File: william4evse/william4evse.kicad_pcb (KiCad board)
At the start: 2 copper layers, 34 x 66 mm, 2 parts, among them J1 Boom_Precision_RJ45-B-1x1, U1 RCMB121

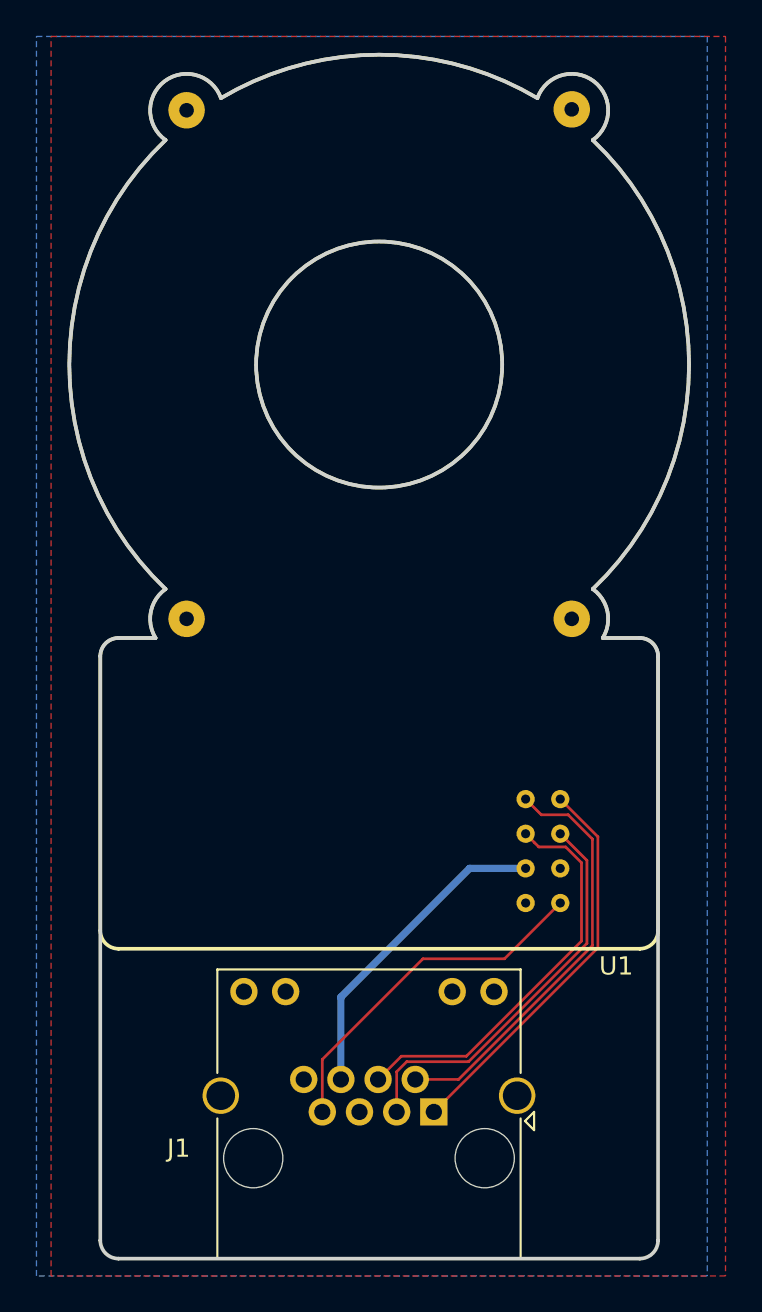
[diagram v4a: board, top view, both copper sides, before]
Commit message: william: Misc updates
- Add power inductor in the power line
- Swap TEST_IN and X30_OUT signals
- Fix board outline to take RCMB bumps into account
- Fix RCMB hole size
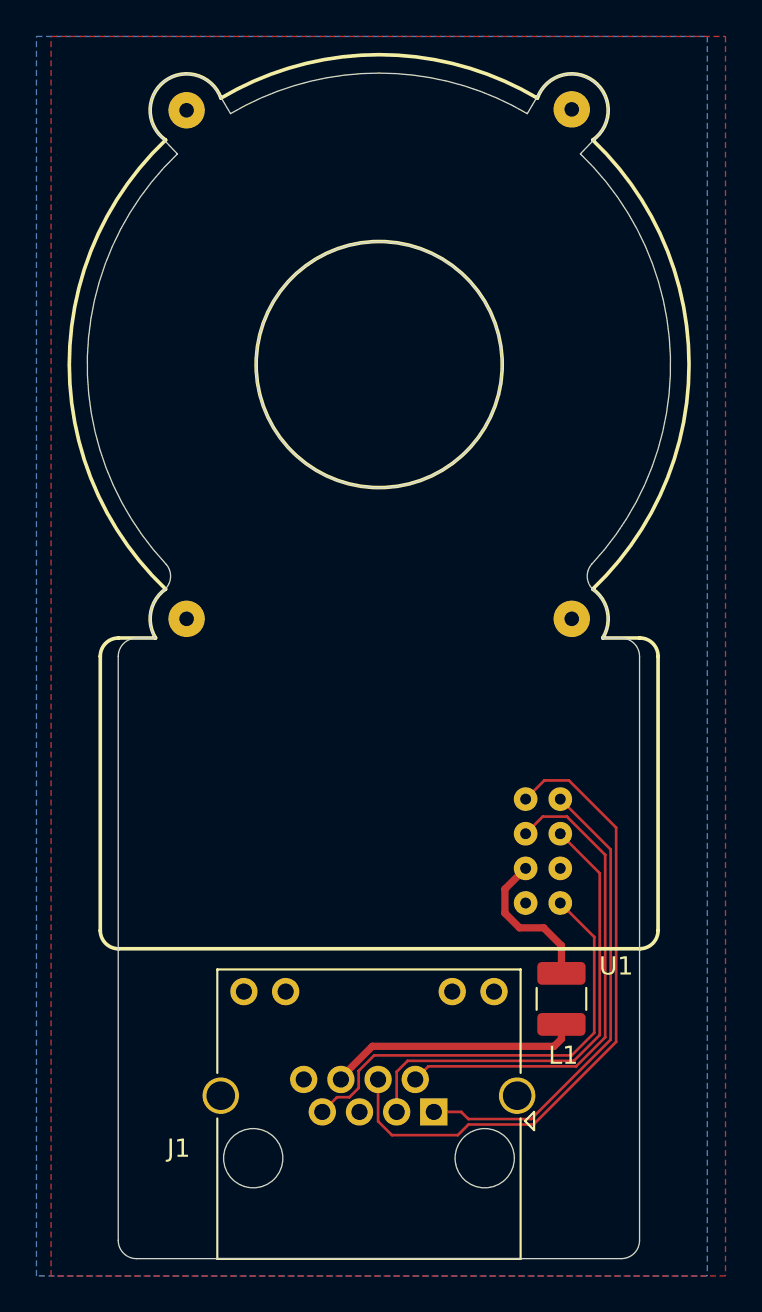
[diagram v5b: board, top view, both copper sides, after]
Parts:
- added L1: 220uH, Inductor_SMD:L_1210_3225Metric, F.Cu at (152.0, 108.8)
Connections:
- J1 pad 2: /TEST_IN -> /X30_OUT
- J1 pad 4: /X30_OUT -> /TEST_IN
- U1 pad 6: +5V -> Net-(L1-Pad2)
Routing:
- net /TEST_IN: track 23.2 -> 36.0 mm
- net Net-(L1-Pad2): track 0.00 -> 8.29 mm
- net /PWM_OUT: track 19.5 -> 25.2 mm
- net /X30_OUT: track 22.3 -> 27.0 mm
- net /ERROR_OUT: track 21.7 -> 26.0 mm
- net /X6_OUT: track 22.2 -> 26.1 mm
- net +5V: track 17.6 -> 13.9 mm
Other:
- board size 34 x 66 mm -> 32 x 65 mm

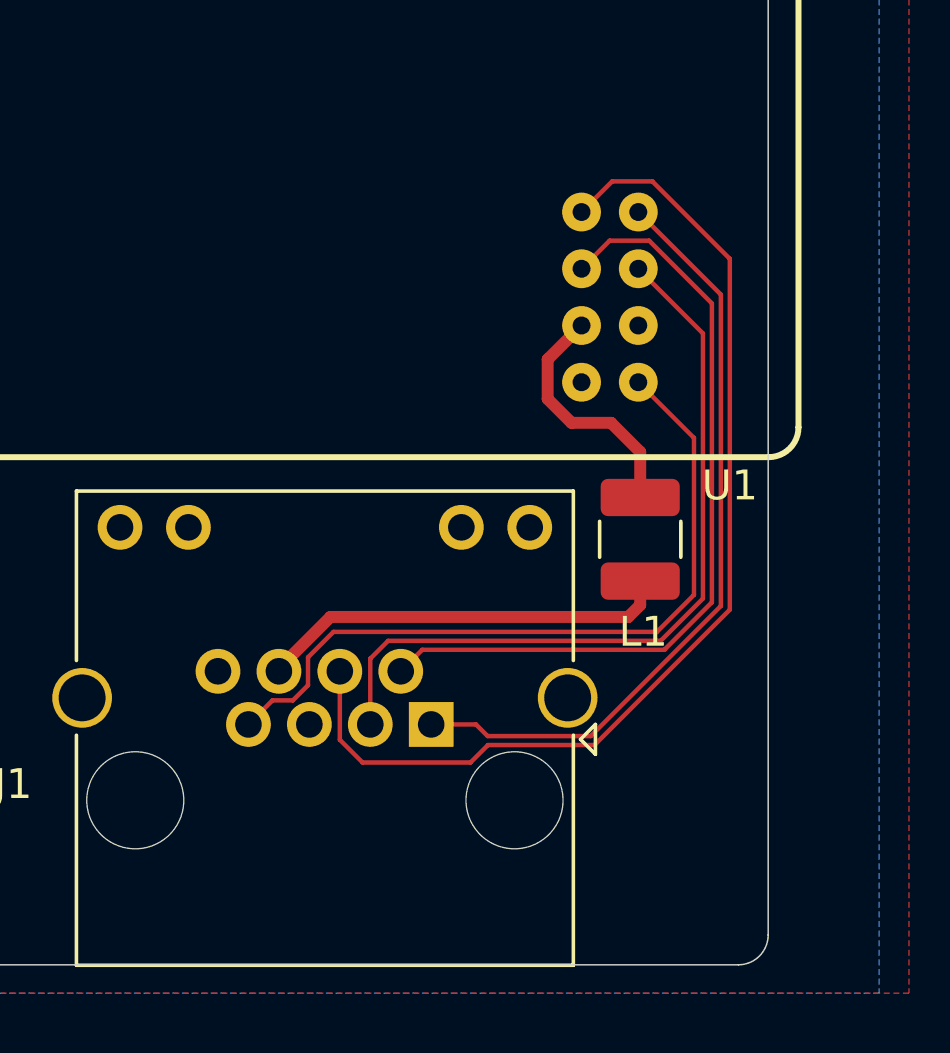
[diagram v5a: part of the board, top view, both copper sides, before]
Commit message: william{sch, pcb}: Swap (again) wires
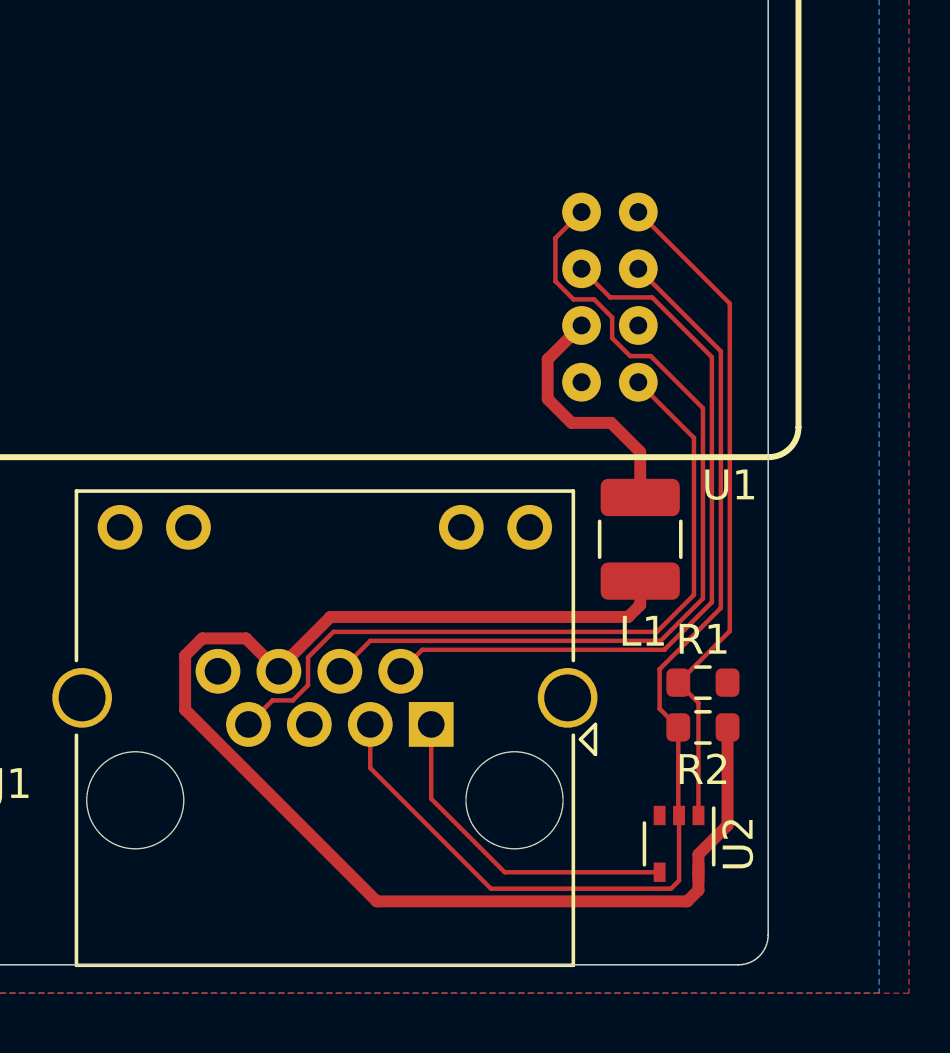
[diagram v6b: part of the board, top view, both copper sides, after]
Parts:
- added R1: 10k, Resistor_SMD:R_0603_1608Metric, F.Cu at (154.1, 113.6)
- added R2: 10k, Resistor_SMD:R_0603_1608Metric, F.Cu at (154.1, 115.1)
- added U2: 74LVC1G32, Package_TO_SOT_SMD:SOT-353_SC-70-5, F.Cu at (153.3, 119.0)
- L1: value 220uH -> 330u
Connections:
- J1 pad 1: /ERROR_OUT -> /FAULT_OUT
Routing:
- net +5V: track 13.9 -> 45.4 mm
- net /FAULT_OUT: track 0.00 -> 11.2 mm
- net /X6_OUT: track 26.1 -> 36.3 mm
- net /TEST_IN: track 36.0 -> 29.3 mm
- net /ERROR_OUT: track 26.0 -> 22.5 mm
- net /X30_OUT: track 27.0 -> 25.2 mm

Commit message: william: Release v1.2
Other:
- board text added: "Dalton EVSE "William" board rev. 1.2 (c) Tuetuopay 2019 - 2020"
- board text removed: "Dalton EVSE "William" board rev. 1.1 (c) Tuetuopay 2019 - 2020"
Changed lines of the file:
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@@
     (effects (font (size 1 1) (thickness 0.15)) (justify left mirror))
   )
-  (gr_text "Dalton EVSE\n\"William\" board rev. 1.1\n(c) Tuetuopay 2019 - 2020" (at 150 92) (layer B.SilkS)
+  (gr_text "Dalton EVSE\n\"William\" board rev. 1.2\n(c) Tuetuopay 2019 - 2020" (at 150 92) (layer B.SilkS)
     (effects (font (size 1 1) (thickness 0.15)) (justify left mirror))
   )

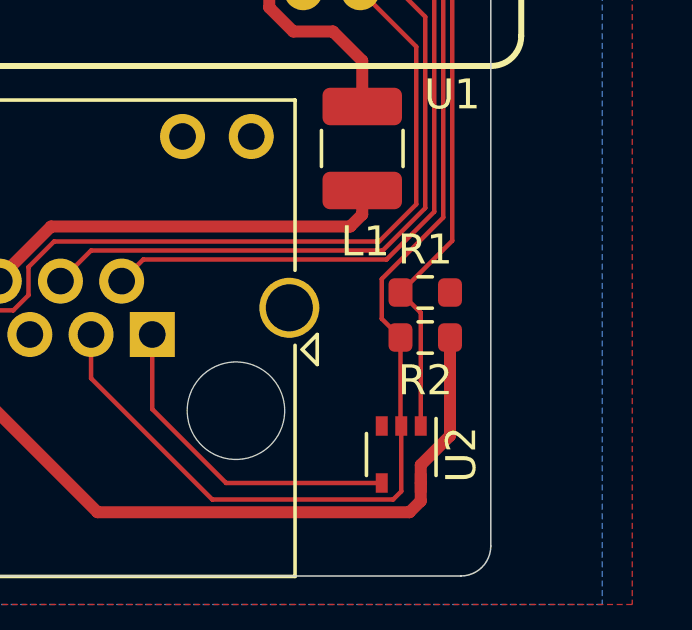
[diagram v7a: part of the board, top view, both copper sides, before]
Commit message: william/pcb: Fix missing 5V trace
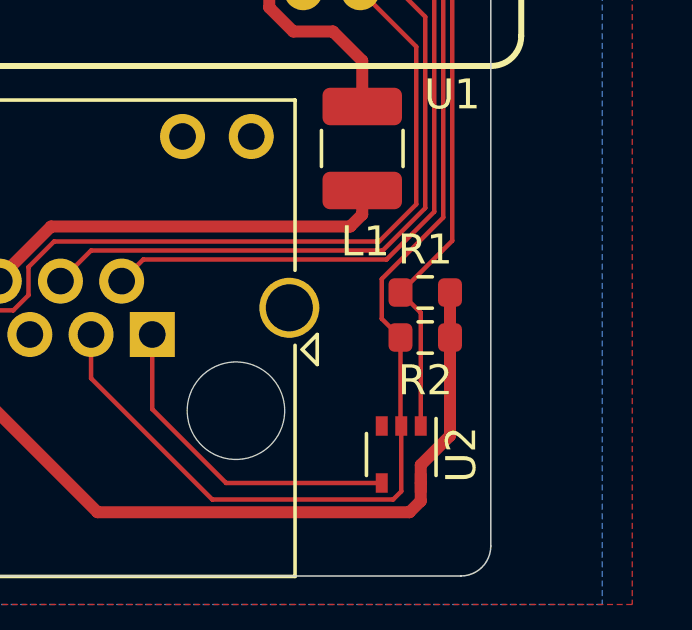
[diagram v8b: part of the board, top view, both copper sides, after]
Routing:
- net +5V: track 45.4 -> 46.9 mm
